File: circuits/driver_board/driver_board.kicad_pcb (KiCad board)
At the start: 2 copper layers, 29 parts, among them P1 CONN_01X06, P2 CONN_01X07, Q1 C5468, U1 74LS244, U2 74HC04, U3 7805

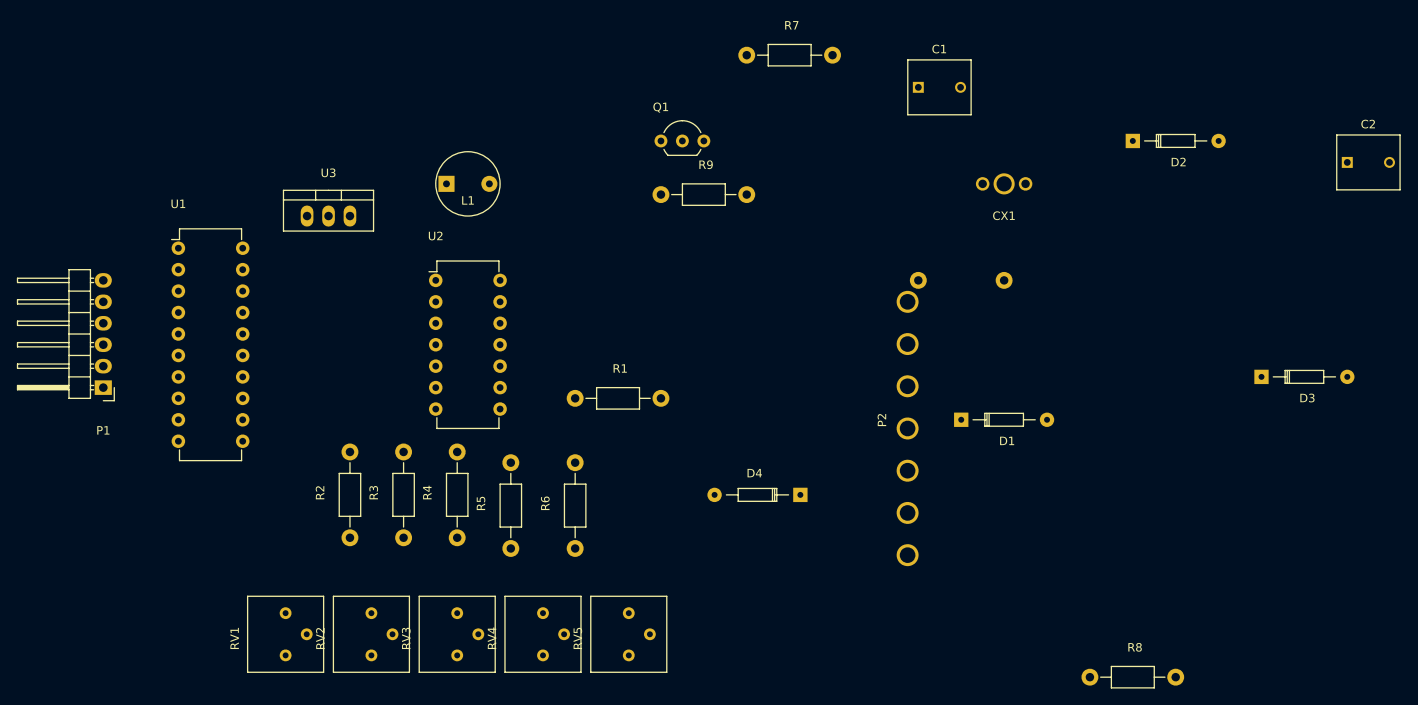
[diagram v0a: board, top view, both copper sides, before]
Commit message: Continuing to work on dts for lcd
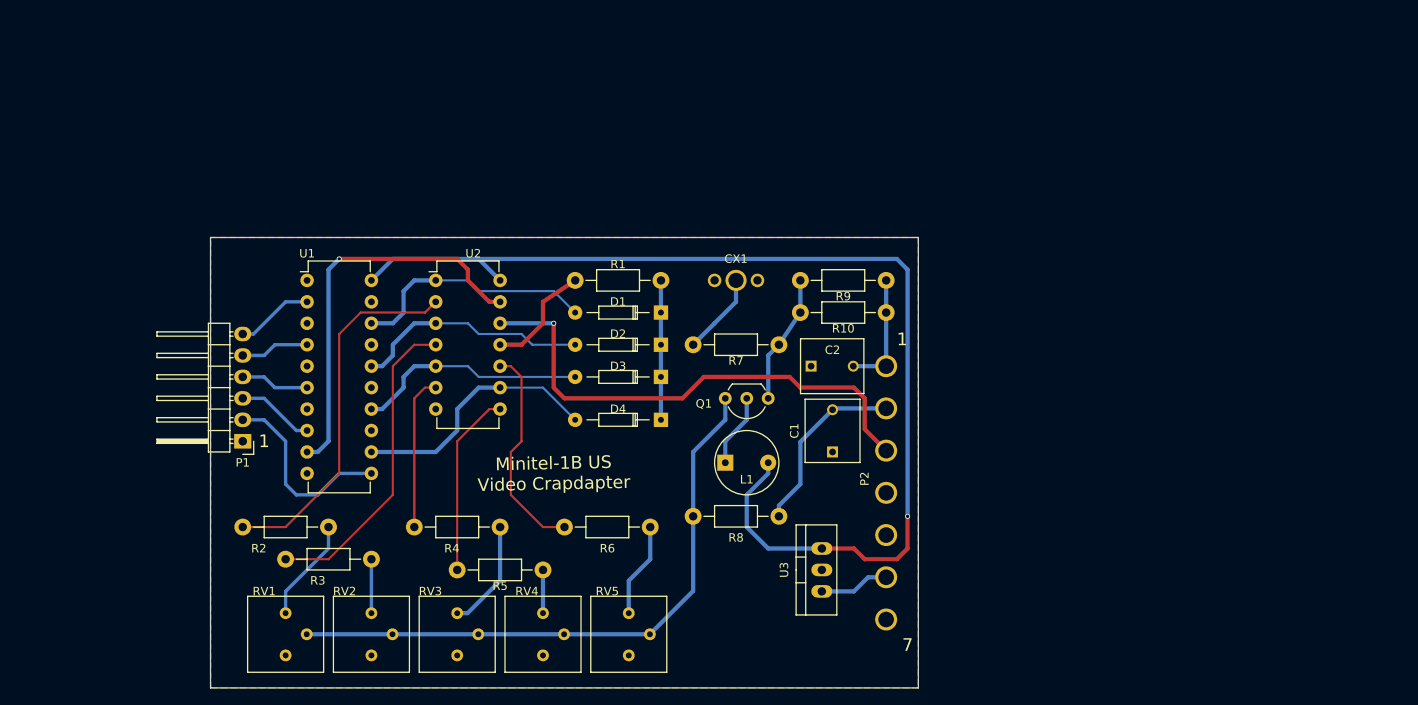
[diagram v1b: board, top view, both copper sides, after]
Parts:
- R10: moved to F.Cu
- moved U3 71.9 mm to (176.5, 133.3), turned to 90 degrees
- moved D3 71.1 mm to (157.5, 110.5), turned to 180 degrees
- moved C2 67.9 mm to (175.3, 109.2)
- moved D2 60.9 mm to (157.5, 106.7), turned to 180 degrees
- moved L1 46.7 mm to (167.6, 120.7)
- moved C1 44.4 mm to (177.8, 119.4), turned to 90 degrees
- moved R8 41.5 mm to (171.4, 127.0), turned to 180 degrees
- moved D1 37.8 mm to (157.5, 102.9), turned to 180 degrees
- moved R7 34.9 mm to (161.3, 106.7)
- moved CX1 33.7 mm to (166.4, 102.9)
- moved Q1 33.0 mm to (170.2, 113.0), turned to 180 degrees
- moved R9 28.5 mm to (184.2, 99.1), turned to 180 degrees
- moved D4 18.8 mm to (157.5, 115.6)
- moved P1 17.7 mm to (108.0, 118.1)
- moved U1 15.7 mm to (115.6, 99.1)
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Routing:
- net VCC: track 0.00 -> 131.5 mm, vias 0 -> 1
- net Net-(Q1-Pad3): track 0.00 -> 72.3 mm
- net Net-(P2-Pad3): track 0.00 -> 60.7 mm, vias 0 -> 1
- net SYNC: track 0.00 -> 47.1 mm, vias 0 -> 1
- net Net-(R2-Pad2): track 0.00 -> 43.6 mm
- net Net-(R3-Pad2): track 0.00 -> 37.2 mm
- net Net-(D4-Pad2): track 0.00 -> 30.4 mm
- net Net-(D1-Pad2): track 0.00 -> 29.3 mm
- net Net-(D2-Pad2): track 0.00 -> 28.0 mm
- net Net-(D3-Pad2): track 0.00 -> 27.5 mm
- net Net-(R6-Pad2): track 0.00 -> 25.5 mm
- net Net-(P1-Pad2): track 0.00 -> 23.0 mm
- net Net-(C1-Pad2): track 0.00 -> 22.2 mm
- net Net-(R5-Pad2): track 0.00 -> 21.9 mm
- net Net-(R4-Pad2): track 0.00 -> 18.3 mm
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- added copper zone on F.Cu, net GND
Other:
- board outline added: 83.8 x 53.3 mm
- net class Default: clearance 0.2 -> 0.25
- net class normal added: clearance 0.4, trace_width 0.4, via_dia 0.6, via_drill 0.4
- rule trace_clearance: 0.2 -> 0.25
- board text added: "1"
- board text added: "7"
- board text added: "Minitel-1B US Video Crapdapter"
